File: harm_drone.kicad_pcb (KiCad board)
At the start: 4 copper layers, 100 x 40 mm, 62 parts, among them IC1 Microcontroller, IC2 USB Hub, IC3 SRAM, IC4 LDO, J1 SYS_DEBUG, J2 2-Port USB, J3 2-Port USB, J4 SD_Card, J5 SPI2, J6 SPI1, J7 XT60-M, U1 LMR51430, U2 EEPROM

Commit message: final changes
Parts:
- removed the C15 at (132.8, 98.2)
- removed the C16 at (132.8, 95.7)
- removed the C17 at (137.8, 97.2)
- removed the C18 at (140.2, 97.2)
- removed the C19 at (145.2, 87.7)
- removed the C20 at (145.2, 85.2)
- removed the C21 at (132.7, 81.7)
- removed the C22 at (135.2, 81.7)
- removed the C23 at (97.7, 116.5)
- added C10: 0.1uF, Capacitor_SMD:C_0805_2012Metric, F.Cu at (132.5, 98.2)
- added C11: 4.7uF, Capacitor_SMD:C_0805_2012Metric, F.Cu at (134.8, 98.2)
- added C12: 0.1uF, Capacitor_SMD:C_0805_2012Metric, F.Cu at (141.3, 86.5)
- added C13: 4.7uF, Capacitor_SMD:C_0805_2012Metric, F.Cu at (141.3, 84.2)
- added C2: 0.1uF, Capacitor_SMD:C_0805_2012Metric, F.Cu at (136.2, 82.2)
- added C25: 2.2uF, Capacitor_SMD:C_0805_2012Metric, F.Cu at (117.8, 82.5)
- added C26: 2.2uF, Capacitor_SMD:C_0805_2012Metric, F.Cu at (107.2, 82.5)
- added C3: 0.1uF, Capacitor_SMD:C_0805_2012Metric, F.Cu at (134.0, 82.2)
- added C4: 10nF, Capacitor_SMD:C_0805_2012Metric, F.Cu at (126.2, 92.5)
- added C5: 0.1uF, Capacitor_SMD:C_0805_2012Metric, F.Cu at (129.5, 82.2)
- added C6: 0.1uF, Capacitor_SMD:C_0805_2012Metric, F.Cu at (122.5, 92.5)
- added C7: 4.7uF, Capacitor_SMD:C_0805_2012Metric, F.Cu at (131.7, 82.2)
- added C8: 0.1uF, Capacitor_SMD:C_0805_2012Metric, F.Cu at (137.0, 98.2)
- added C9: 0.1uF, Capacitor_SMD:C_0805_2012Metric, F.Cu at (139.2, 98.2)
- added R10: 15kOhm, Resistor_SMD:R_0805_2012Metric, F.Cu at (164.2, 105.8)
- added R11: 15kOhm, Resistor_SMD:R_0805_2012Metric, F.Cu at (155.2, 115.8)
- added R12: 15kOhm, Resistor_SMD:R_0805_2012Metric, F.Cu at (173.5, 103.0)
- added R13: 15kOhm, Resistor_SMD:R_0805_2012Metric, F.Cu at (159.2, 113.8)
- added R14: 15kOhm, Resistor_SMD:R_0805_2012Metric, F.Cu at (176.2, 100.0)
- added R15: 15kOhm, Resistor_SMD:R_0805_2012Metric, F.Cu at (159.2, 110.2)
- added R16: 15kOhm, Resistor_SMD:R_0805_2012Metric, F.Cu at (178.5, 96.8)
- added R2: 27ohm, Resistor_SMD:R_0805_2012Metric, F.Cu at (150.2, 111.8)
- added R3: 27ohm, Resistor_SMD:R_0805_2012Metric, F.Cu at (154.5, 113.0)
- added R4: 27ohm, Resistor_SMD:R_0805_2012Metric, F.Cu at (154.5, 111.0)
- added R5: 27ohm, Resistor_SMD:R_0805_2012Metric, F.Cu at (156.7, 105.4)
- added R6: 27ohm, Resistor_SMD:R_0805_2012Metric, F.Cu at (156.7, 103.4)
- added R7: 27ohm, Resistor_SMD:R_0805_2012Metric, F.Cu at (157.5, 101.2)
- added R8: 27ohm, Resistor_SMD:R_0805_2012Metric, F.Cu at (157.5, 99.2)
- added R9: 15kOhm, Resistor_SMD:R_0805_2012Metric, F.Cu at (149.5, 117.0)
- C24: value 0.1uF -> 2.2uF
- R1: value 2kOhm -> 27ohm
- R21: renamed from R6; value 27 -> 27ohm
- moved C18 29.3 mm to (162.6, 80.5), turned to 180 degrees
- moved C23 25.4 mm to (162.6, 92.5), turned to 180 degrees
- moved C22 24.9 mm to (162.6, 90.0), turned to 180 degrees
- moved IC3 24.8 mm to (162.6, 84.0), turned to -90 degrees
- moved R24 23.7 mm to (116.0, 116.0), turned to -90 degrees
- moved R23 23.3 mm to (116.0, 112.2), turned to -90 degrees
- moved R22 22.9 mm to (116.0, 108.8), turned to -90 degrees
- moved C19 21.6 mm to (162.6, 87.5), turned to 180 degrees
- moved R20 20.0 mm to (116.0, 105.2)
- moved C17 18.6 mm to (151.5, 97.5), turned to 90 degrees
- moved C16 17.5 mm to (153.7, 97.5), turned to 90 degrees
- moved R19 16.7 mm to (97.5, 108.2)
- moved R17 14.1 mm to (158.5, 93.2)
- moved IC2 13.2 mm to (149.5, 104.5)
- moved J1 13.1 mm to (143.2, 94.5), turned to 180 degrees
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- renumbered C2 to C14, C3 to C15, C4 to C16, C5 to C17, C6 to C18, C7 to C19, C8 to C20, C9 to C21, C10 to C22, C11 to C23, C12 to C27, C13 to C28, C14 to C29, IC4 to IC3, IC3 to IC4, J7 to J4, J4 to J5, J5 to J6, J6 to J7, R2 to R17, R3 to R18, R4 to R19, R5 to R20, R7 to R22, R8 to R23, R9 to R24, R10 to R25, R11 to R26, R12 to R27, R13 to R28, R14 to R29, R15 to R30
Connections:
- C24 pad 1: GND -> 3V3
- C24 pad 2: 3V3 -> GND
- IC1 pad 1: 3V3 -> unconnected-(IC1-VBAT-Pad1)
- IC2 pad 8: Net-(IC2-BUSPWR) -> GND
- J2 pad 2: /USB/D1- -> /USB/J2_D1-
- J2 pad 3: /USB/D1+ -> /USB/J2_D1+
- J2 pad 6: /USB/D2- -> /USB/J2_D2-
- J2 pad 7: /USB/D2+ -> /USB/J2_D2+
- J3 pad 2: /USB/D3- -> /USB/J3_D1-
- J3 pad 3: /USB/D3+ -> /USB/J3_D1+
- J3 pad 6: /USB/D4- -> /USB/J3_D2-
- J3 pad 7: /USB/D4+ -> /USB/J3_D2+
- R1 pad 1: Net-(IC2-BUSPWR) -> /USB/D1-
- R1 pad 2: GND -> /USB/J2_D1-
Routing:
- net /USB/J2_D1-: track 0.00 -> 59.0 mm, vias 0 -> 1
- net /USB/J2_D1+: track 0.00 -> 56.1 mm, vias 0 -> 1
- net SPI CLOCK 2: track 62.8 -> 96.8 mm, vias 0 -> 2
- net /USB/J3_D2-: track 0.00 -> 30.5 mm
- net /USB/J3_D2+: track 0.00 -> 30.1 mm
- net 5V: track 133.5 -> 161.3 mm, vias 2 -> 5
- net /USB/J3_D1+: track 0.00 -> 27.6 mm
- net /USB/J3_D1-: track 0.00 -> 26.3 mm
- net CS EEPROM: track 44.3 -> 69.5 mm, vias 0 -> 2
- net RXD_USB2SERIAL: track 42.7 -> 20.1 mm, vias 0 -> 2
- net /USB/D4-: track 25.4 -> 3.40 mm, vias 1 -> 0
- net Net-(U1-SW): track 17.2 -> 38.8 mm
- net /USB/D4+: track 25.3 -> 3.89 mm, vias 1 -> 0
- net /USB/J2_D2+: track 0.00 -> 17.5 mm
- net /USB/J2_D2-: track 0.00 -> 15.9 mm
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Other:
- board size 100 x 40 mm -> 95.5 x 40.3 mm

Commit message: USB stack changes
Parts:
- added C30: 27pF, Capacitor_SMD:C_0805_2012Metric, F.Cu at (145.8, 116.5)
- added C31: 27pF, Capacitor_SMD:C_0805_2012Metric, F.Cu at (148.5, 115.5)
- added J8: USB_Headers, Connector_PinHeader_2.54mm:PinHeader_1x04_P2.54mm_Vertical, F.Cu at (141.8, 105.2)
- added R31: 1.5kOhm, Resistor_SMD:R_0805_2012Metric, F.Cu at (142.8, 117.2)
- added Y1: ECS-060-20-4X-DU, group127:XTAL_ECS-160-20-4X, F.Cu at (137.2, 106.6)
- moved C14 7.84 mm to (145.2, 113.5)
- moved C15 7.84 mm to (145.2, 111.0)
- moved C27 3.22 mm to (132.8, 106.2), turned to 90 degrees
- moved R9 0.98 mm to (150.3, 117.5)
- moved S2 0.55 mm to (136.2, 116.6)
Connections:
- C29 pad 2: 5V -> Net-(USB-C1-VBUS)
- IC1 pad 29: TSTPLL/48MCLK -> unconnected-(IC1-PA8-Pad29)
- IC1 pad 32: D0- -> unconnected-(IC1-PA11-Pad32)
- IC1 pad 33: D0+ -> unconnected-(IC1-PA12-Pad33)
- IC2 pad 1: D0+ -> Net-(IC2-D0+)
- IC2 pad 2: D0- -> Net-(IC2-D0-)
- IC2 pad 27: TSTPLL/48MCLK -> GND
- IC2 pad 29: unconnected-(IC2-XTAL2-Pad29) -> Net-(IC2-XTAL2)
- IC2 pad 30: 3V3 -> Net-(IC2-XTAL1)
- IC2 pad 31: 3V3 -> GND
- USB2UART1 pad 15: 5V -> Net-(USB-C1-VBUS)
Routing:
- net Net-(IC2-XTAL1): track 0.00 -> 34.1 mm, vias 0 -> 1
- net Net-(USB-C1-VBUS): track 21.4 -> 42.5 mm
- net Net-(IC2-XTAL2): track 0.00 -> 20.0 mm, vias 0 -> 2
- net TSTPLL/48MCLK: track 19.0 -> 0.00 mm, vias 2 -> 0
- net GND: track 2.86 -> 21.9 mm, vias 67 -> 72
- net D0-: track 18.4 -> 0.00 mm
- net D0+: track 18.1 -> 0.00 mm
- net Net-(C30-Pad1): track 0.00 -> 13.7 mm
- net 5V: track 161.3 -> 148.1 mm, vias 5 -> 2
- net Net-(IC2-D0-): track 0.00 -> 9.27 mm, vias 0 -> 1
- net Net-(IC2-D0+): track 0.00 -> 7.54 mm, vias 0 -> 1
- net 3V3: track 9.40 -> 8.60 mm, vias 39 -> 38
- net /USB-Serial/USBD-: track 18.9 -> 19.4 mm

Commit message: final changes to 3d models
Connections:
- net Net-(IC1-PA13) renamed SWDIO
- net Net-(IC1-PA14) renamed SWCLK
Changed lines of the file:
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@@
 	(net 38 "unconnected-(IC1-VBAT-Pad1)")
 	(net 39 "Net-(C30-Pad1)")
-	(net 40 "Net-(IC1-PA14)")
+	(net 40 "SWCLK")
 	(net 41 "unconnected-(IC1-PA3-Pad13)")
 	(net 42 "~{USB_RESET}")
-	(net 43 "Net-(IC1-PA13)")
+	(net 43 "SWDIO")
 	(net 44 "MOSI 1")
 	(net 45 "unconnected-(IC1-PB7-Pad43)")
@@
 			(pintype "power_in")
 		)
-		(model "IS62WVS2568GBLL-45NLI-TR.stp"
+		(model "/models/IS62WVS2568GBLL-45NLI-TR.stp"
 			(offset
 				(xyz 0 0 0)
@@
 			(layers "*.Cu" "*.Mask")
 			(remove_unused_layers no)
-			(net 43 "Net-(IC1-PA13)")
+			(net 43 "SWDIO")
 			(pinfunction "Pin_2")
 			(pintype "passive")
@@
 			(layers "*.Cu" "*.Mask")
 			(remove_unused_layers no)
-			(net 40 "Net-(IC1-PA14)")
+			(net 40 "SWCLK")
 			(pinfunction "Pin_3")
 			(pintype "passive")
@@
 			(solder_mask_margin 0.102)
 		)
+		(model "/models/ECS-060-20-4X-DU.step"
+			(offset
+				(xyz -0.2 0 0)
+			)
+			(scale
+				(xyz 1 1 1)
+			)
+			(rotate
+				(xyz -90 0 0)
+			)
+		)
 	)
 	(footprint "Resistor_SMD:R_0805_2012Metric"
@@
 			(pintype "passive")
 		)
-		(model "KSR221GLFS.stp"
+		(model "/models/KSR221GLFS.stp"
 			(offset
 				(xyz 0 0 0)
@@
 		(tags "Through hole pin header THT 1x04 2.54mm single row")
 		(property "Reference" "J8"
-			(at 0 -2.33 360)
+			(at 0 -2.33 0)
 			(layer "F.SilkS")
 			(effects
@@
 		)
 		(property "Value" "USB_Headers"
-			(at 0 9.950001 360)
+			(at 0 9.950001 0)
 			(layer "F.Fab")
 			(effects
@@
 		(tags "resistor")
 		(property "Reference" "R31"
-			(at 0 -1.65 360)
+			(at 0 -1.65 0)
 			(layer "F.SilkS")
 			(effects
@@
 		)
 		(property "Value" "1.5kOhm"
-			(at 0 1.65 360)
+			(at 0 1.65 0)
 			(layer "F.Fab")
 			(effects
@@
 		)
 		(fp_text user "${REFERENCE}"
-			(at 0 0 360)
+			(at 0 0 0)
 			(layer "F.Fab")
 			(effects
@@
 			(pintype "passive")
 		)
-		(model "7447707068.stp"
+		(model "/models/7447707068.stp"
 			(offset
 				(xyz 0 0 0)
@@
 			(pintype "power_in")
 		)
+		(model "/models/IS62WVS2568GBLL-45NLI-TR.stp"
+			(offset
+				(xyz 0 0 0)
+			)
+			(scale
+				(xyz 1 1 1)
+			)
+			(rotate
+				(xyz 0 0 0)
+			)
+		)
 	)
 	(footprint "Capacitor_SMD:C_0805_2012Metric"
@@
 			(size 0.3 1.475)
 			(layers "F.Cu" "F.Paste" "F.Mask")
-			(net 43 "Net-(IC1-PA13)")
+			(net 43 "SWDIO")
 			(pinfunction "PA13")
 			(pintype "passive")
@@
 			(size 0.3 1.475)
 			(layers "F.Cu" "F.Paste" "F.Mask")
-			(net 40 "Net-(IC1-PA14)")
+			(net 40 "SWCLK")
 			(pinfunction "PA14")
 			(pintype "passive")
@@
 			(pintype "passive")
 		)
-		(model "LQFP48-7x7mm.step"
+		(model "/models/LQFP48-7x7mm.step"
 			(offset
 				(xyz 0 0 0)

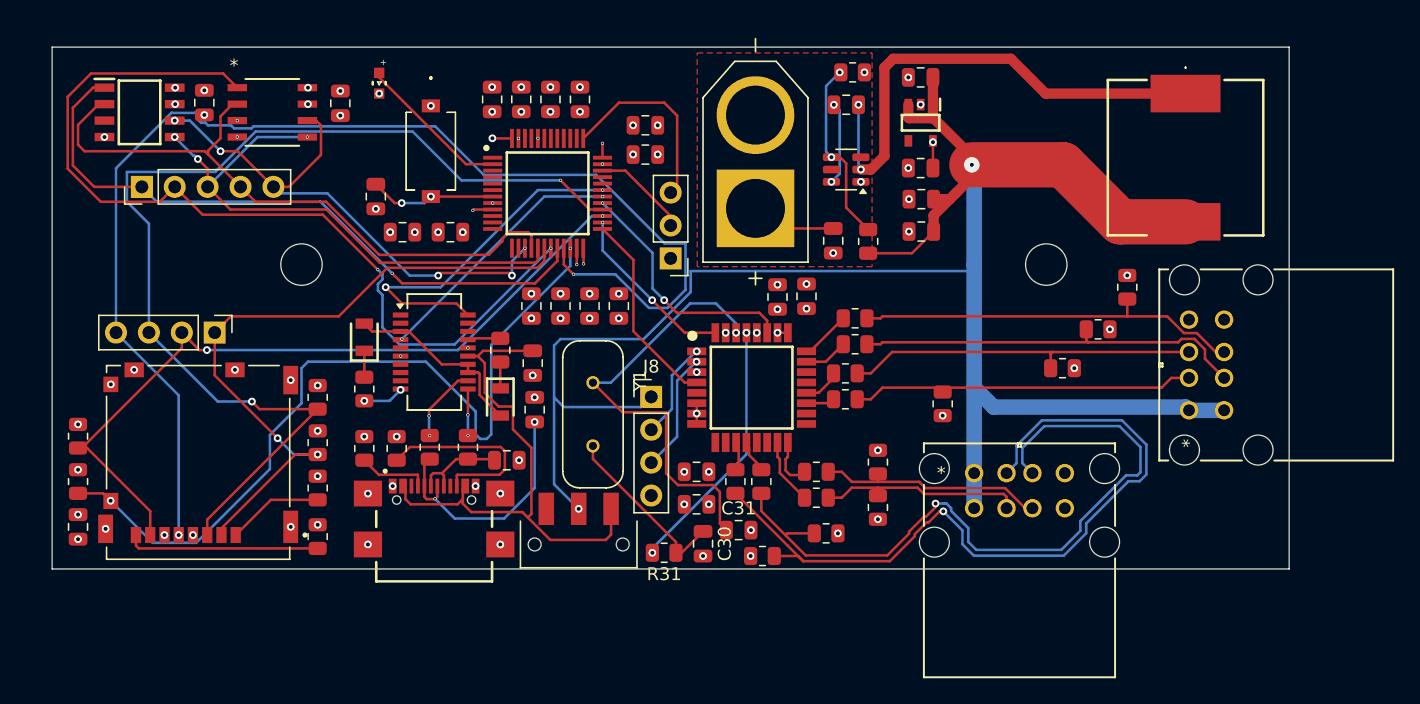
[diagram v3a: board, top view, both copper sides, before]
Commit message: USB fixes
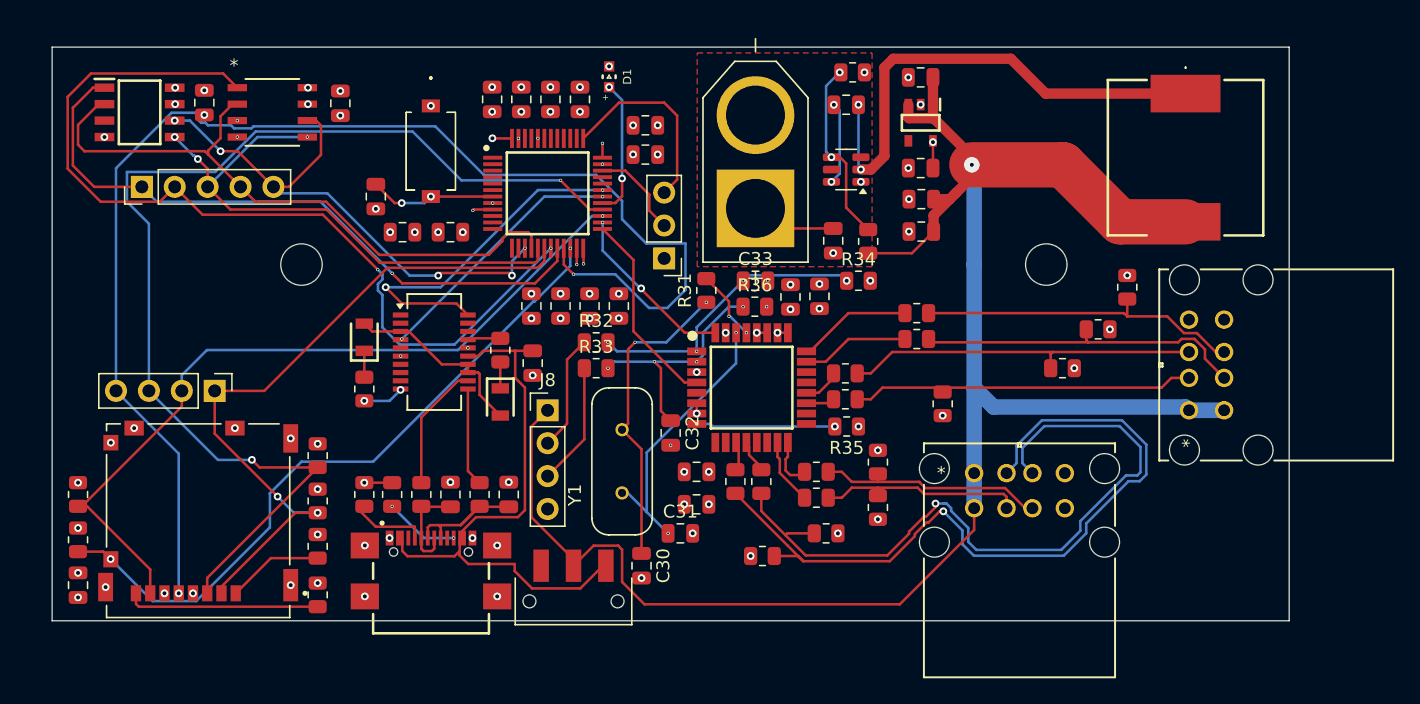
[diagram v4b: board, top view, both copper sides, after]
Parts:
- added C32: 22pF, Capacitor_SMD:C_0805_2012Metric, F.Cu at (143.2, 108.0)
- added C33: 22pF, Capacitor_SMD:C_0805_2012Metric, F.Cu at (149.8, 96.2)
- added R32: 27ohm, Resistor_SMD:R_0805_2012Metric, F.Cu at (137.5, 101.0)
- added R33: 27ohm, Resistor_SMD:R_0805_2012Metric, F.Cu at (137.5, 103.0)
- added R34: 1.5kOhm, Resistor_SMD:R_0805_2012Metric, F.Cu at (157.8, 96.2)
- added R35: 1.5kOhm, Resistor_SMD:R_0805_2012Metric, F.Cu at (156.8, 107.5)
- added R36: 1.5kOhm, Resistor_SMD:R_0805_2012Metric, F.Cu at (149.8, 98.2)
- moved R31 20.5 mm to (146.0, 97.0), turned to 90 degrees
- moved D1 17.8 mm to (138.5, 80.5), turned to -90 degrees
- moved C27 9.23 mm to (126.2, 112.8)
- moved J8 8.07 mm to (133.8, 106.2)
- moved C30 5.05 mm to (141.0, 118.2)
- moved R7 4.78 mm to (162.2, 100.8)
- moved R8 4.78 mm to (162.2, 98.8)
- moved C31 4.51 mm to (144.0, 115.8)
- moved C24 4.50 mm to (97.5, 119.8)
- moved J5 4.50 mm to (106.8, 114.8)
- moved J6 4.50 mm to (108.0, 104.8)
- moved R19 4.50 mm to (97.5, 112.8)
- moved R20 4.50 mm to (116.0, 109.8)
- moved R21 4.50 mm to (97.5, 116.2)
- moved R22 4.50 mm to (116.0, 113.2)
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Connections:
- net SWCLK renamed Net-(IC1-PA14)
- net SWDIO renamed Net-(IC1-PA13)
- D1 pad 2: Net-(IC1-PC13) -> Net-(IC1-PA8)
- IC1 pad 2: Net-(IC1-PC13) -> unconnected-(IC1-PC13-Pad2)
- IC1 pad 29: unconnected-(IC1-PA8-Pad29) -> Net-(IC1-PA8)
- IC2 pad 8: GND -> Net-(IC2-BUSPWR)
- J8 pad 2: Net-(IC2-D0+) -> Net-(J8-Pin_2)
- J8 pad 3: Net-(IC2-D0-) -> Net-(J8-Pin_3)
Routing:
- net GND: track 21.9 -> 5.01 mm
- net Net-(IC2-D0+): track 7.54 -> 22.4 mm, vias 1 -> 4
- net Net-(IC2-XTAL2): track 20.0 -> 5.51 mm
- net Net-(IC2-XTAL1): track 34.1 -> 21.5 mm, vias 1 -> 2
- net Net-(IC1-PC13): track 11.9 -> 0.00 mm
- net /USB-Serial/USBD-: track 19.4 -> 7.62 mm, vias 2 -> 0
- net Net-(IC2-BUSPWR): track 0.00 -> 10.7 mm, vias 0 -> 2
- net Net-(IC1-PA8): track 0.00 -> 10.6 mm, vias 0 -> 2
- net Net-(C30-Pad1): track 13.7 -> 24.1 mm, vias 0 -> 2
- net CARD_DETECT: track 63.0 -> 53.2 mm
- net Net-(J8-Pin_3): track 0.00 -> 9.51 mm
- net Net-(USB-C1-CC2): track 15.1 -> 5.76 mm, vias 0 -> 2
- net Net-(IC2-D0-): track 9.27 -> 18.5 mm, vias 1 -> 4
- net Net-(J8-Pin_2): track 0.00 -> 8.97 mm
- net SPI CLOCK 2: track 96.8 -> 102.1 mm
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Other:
- board size 95.5 x 40.3 mm -> 95.5 x 44.3 mm

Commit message: overcurrent fixes
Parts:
- R35: value 1.5kOhm -> 2kOhm
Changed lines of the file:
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@@
 		(tags "resistor")
 		(property "Reference" "R35"
-			(at 0 -1.65 360)
+			(at 0 -1.65 0)
 			(layer "F.SilkS")
 			(effects
@@
 			)
 		)
-		(property "Value" "1.5kOhm"
-			(at 0 1.65 360)
+		(property "Value" "2kOhm"
+			(at 0 1.65 0)
 			(layer "F.Fab")
 			(effects
@@
 		)
 		(fp_text user "${REFERENCE}"
-			(at 0 0 360)
+			(at 0 0 0)
 			(layer "F.Fab")
 			(effects
@@
 		(tags "resistor")
 		(property "Reference" "R34"
-			(at 0 -1.65 360)
+			(at 0 -1.65 0)
 			(layer "F.SilkS")
 			(effects
@@
 		)
 		(property "Value" "1.5kOhm"
-			(at 0 1.65 360)
+			(at 0 1.65 0)
 			(layer "F.Fab")
 			(effects
@@
 		)
 		(fp_text user "${REFERENCE}"
-			(at 0 0 360)
+			(at 0 0 0)
 			(layer "F.Fab")
 			(effects

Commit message: New vias
Added new vias
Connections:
- IC2 pad 10: unconnected-(IC2-~{OVRCUR1}-Pad10) -> 3V3
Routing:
- net 3V3: vias 40 -> 44
